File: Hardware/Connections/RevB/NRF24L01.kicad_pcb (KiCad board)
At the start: 2 copper layers, 30.5 x 28.9 mm, 9 parts, among them P1 CONN_01X09

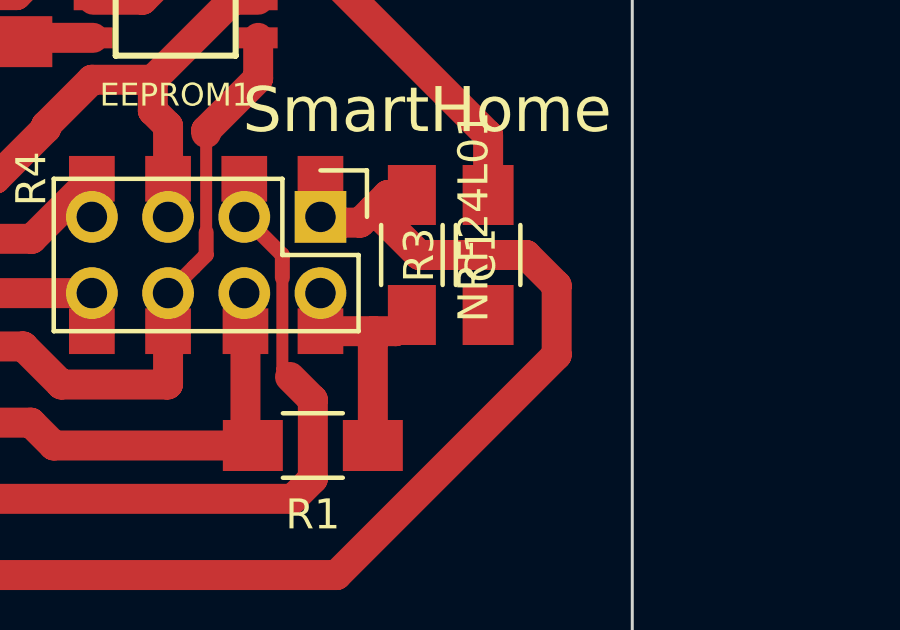
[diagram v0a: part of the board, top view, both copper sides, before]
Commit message: fixed missing wire
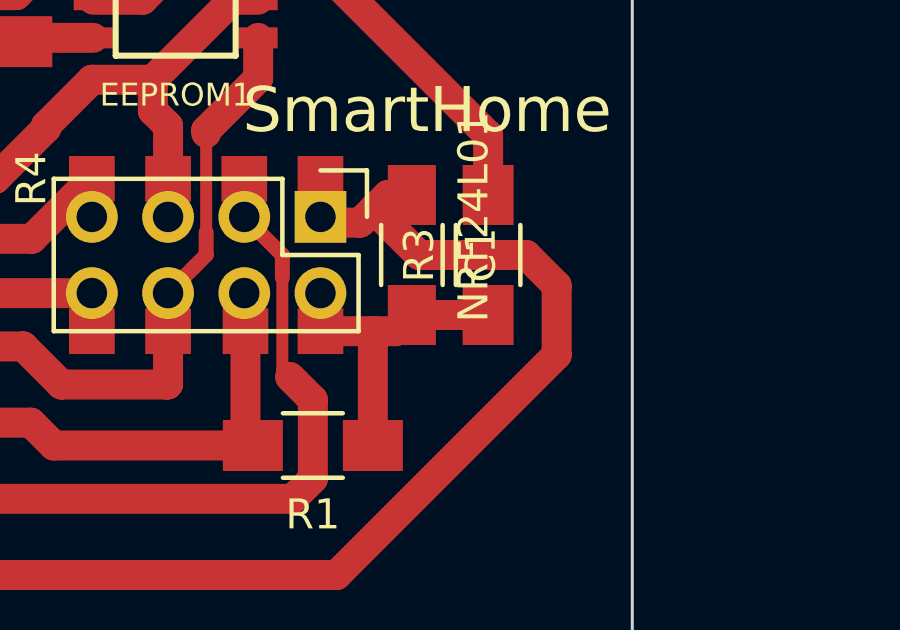
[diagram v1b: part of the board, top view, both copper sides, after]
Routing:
- net Net-(C1-Pad2): track 8.36 -> 10.9 mm
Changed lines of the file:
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@@
   (general
     (links 33)
-    (no_connects 1)
+    (no_connects 0)
     (area 103.378 60.96 174.752001 119.888001)
     (thickness 1.6)
     (drawings 11)
-    (tracks 106)
+    (tracks 107)
     (zones 0)
     (modules 9)
@@
   )
   (setup
-    (last_trace_width 0.5)
+    (last_trace_width 1)
     (user_trace_width 0.4)
     (user_trace_width 1)
@@
       (effects (font (size 1 1) (thickness 0.15)))
     )
-    (fp_text value 0R (at 0 2.3) (layer F.Fab)
+    (fp_text value 0R (at 0.254 0) (layer F.Fab)
       (effects (font (size 1 1) (thickness 0.15)))
     )
@@
       (effects (font (size 1 1) (thickness 0.15)))
     )
-    (fp_text value 0R (at 0 2.3 270) (layer F.Fab)
+    (fp_text value 0R (at 0 0 270) (layer F.Fab)
       (effects (font (size 1 1) (thickness 0.15)))
     )
@@
       (effects (font (size 1 1) (thickness 0.15)))
     )
-    (fp_text value 0R (at 0 2.3 90) (layer F.Fab)
+    (fp_text value 0R (at 0 0.254 90) (layer F.Fab)
       (effects (font (size 1 1) (thickness 0.15)))
     )
@@
       (effects (font (size 1 1) (thickness 0.15)))
     )
-    (fp_text value 10K (at 0 2.3 270) (layer F.Fab)
+    (fp_text value 10K (at -0.254 0 270) (layer F.Fab)
       (effects (font (size 1 1) (thickness 0.15)))
     )
@@
       (effects (font (size 1 1) (thickness 0.15)))
     )
-    (fp_text value 10K (at 0 2.3 180) (layer F.Fab)
+    (fp_text value 10K (at 0 -0.254 180) (layer F.Fab)
       (effects (font (size 1 1) (thickness 0.15)))
     )
@@
       (effects (font (size 1 1) (thickness 0.15)))
     )
-    (fp_text value CONN_01X09 (at 0 -3.1) (layer F.Fab)
+    (fp_text value CONN_01X09 (at -14.732 -3.81) (layer F.Fab)
       (effects (font (size 1 1) (thickness 0.15)))
     )
@@
       (effects (font (size 1 1) (thickness 0.15)))
     )
-    (fp_text value CONN_02X04 (at 0 -3.1 270) (layer F.Fab)
+    (fp_text value CONN_02X04 (at 0.762 -19.812 270) (layer F.Fab)
       (effects (font (size 1 1) (thickness 0.15)))
     )
@@
       (effects (font (size 1 1) (thickness 0.15)))
     )
-    (fp_text value 0.1u (at 0 2.3 270) (layer F.Fab)
+    (fp_text value 0.1u (at -0.254 -0.254 270) (layer F.Fab)
       (effects (font (size 1 1) (thickness 0.15)))
     )
@@
   (segment (start 145.034 90.964) (end 144.230002 90.964) (width 1) (layer F.Cu) (net 1))
   (segment (start 143.308001 91.886001) (end 141.986 91.886001) (width 1) (layer F.Cu) (net 1))
+  (segment (start 147.574 94.964) (end 145.034 94.964) (width 1) (layer F.Cu) (net 2) (status C00000))
   (segment (start 141.986 95.504) (end 143.764 95.504) (width 1) (layer F.Cu) (net 2))
   (segment (start 143.764 95.504) (end 144.494 95.504) (width 1) (layer F.Cu) (net 2))
